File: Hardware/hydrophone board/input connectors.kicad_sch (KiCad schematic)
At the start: 8 parts, among them J5 Conn_01x02, J6 Conn_01x02, J7 Conn_01x02, J8 Conn_01x02

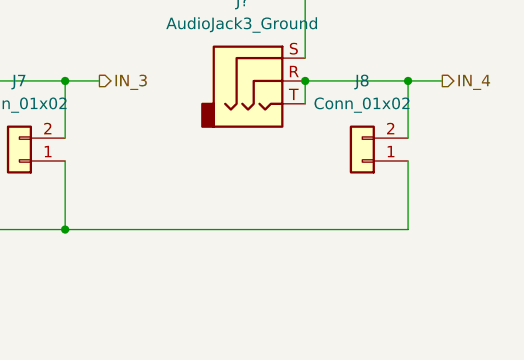
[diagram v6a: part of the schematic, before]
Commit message: moved references, added screw holes
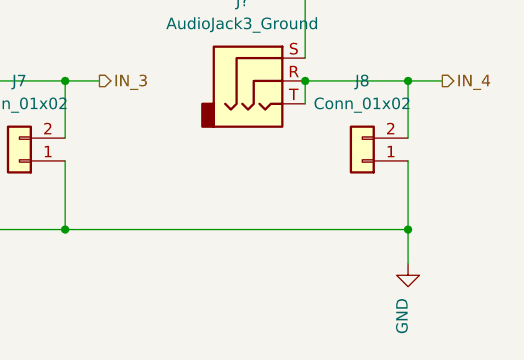
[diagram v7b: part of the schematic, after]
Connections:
- net GND: now also J5.1 (Pin_1), J6.1 (Pin_1), J7.1 (Pin_1), J8.1 (Pin_1)
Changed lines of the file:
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@@
   (junction (at 110.49 86.36) (diameter 0) (color 0 0 0 0)
+  )
+  (junction (at 186.69 86.36) (diameter 0) (color 0 0 0 0)
   )
   (junction (at 148.59 86.36) (diameter 0) (color 0 0 0 0)
@@
   )
   (wire (pts (xy 110.49 69.85) (xy 114.3 69.85))
+    (stroke (width 0) (type default))
+  )
+  (wire (pts (xy 186.69 86.36) (xy 186.69 90.17))
     (stroke (width 0) (type default))
   )
@@
         )
       )
+    )
+  )
+  (symbol (lib_id "power:GND") (at 186.69 90.17 0) (unit 1)
+    (in_bom yes) (on_board yes) (dnp no) (fields_autoplaced)
+    (property "Reference" "#PWR0261" (at 186.69 96.52 0)
+      (effects (font (size 1.27 1.27)) hide)
+    )
+    (property "Value" "GND" (at 186.055 93.98 90)
+      (effects (font (size 1.27 1.27)) (justify right))
+    )
+    (property "Footprint" "" (at 186.69 90.17 0)
+      (effects (font (size 1.27 1.27)) hide)
+    )
+    (property "Datasheet" "" (at 186.69 90.17 0)
+      (effects (font (size 1.27 1.27)) hide)
+    )
+    (pin "1")
+    (instances
+      (project "hydrophone board"
+        (path "/4356d3a6-6a00-447d-897e-473f60221539/1cfbaf71-7039-4355-8fc7-d8c77f0e8058"
+          (reference "#PWR0261") (unit 1)
+        )
+      )
